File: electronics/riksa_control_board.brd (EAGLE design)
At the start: 69.8 x 70.8 mm, 25 parts

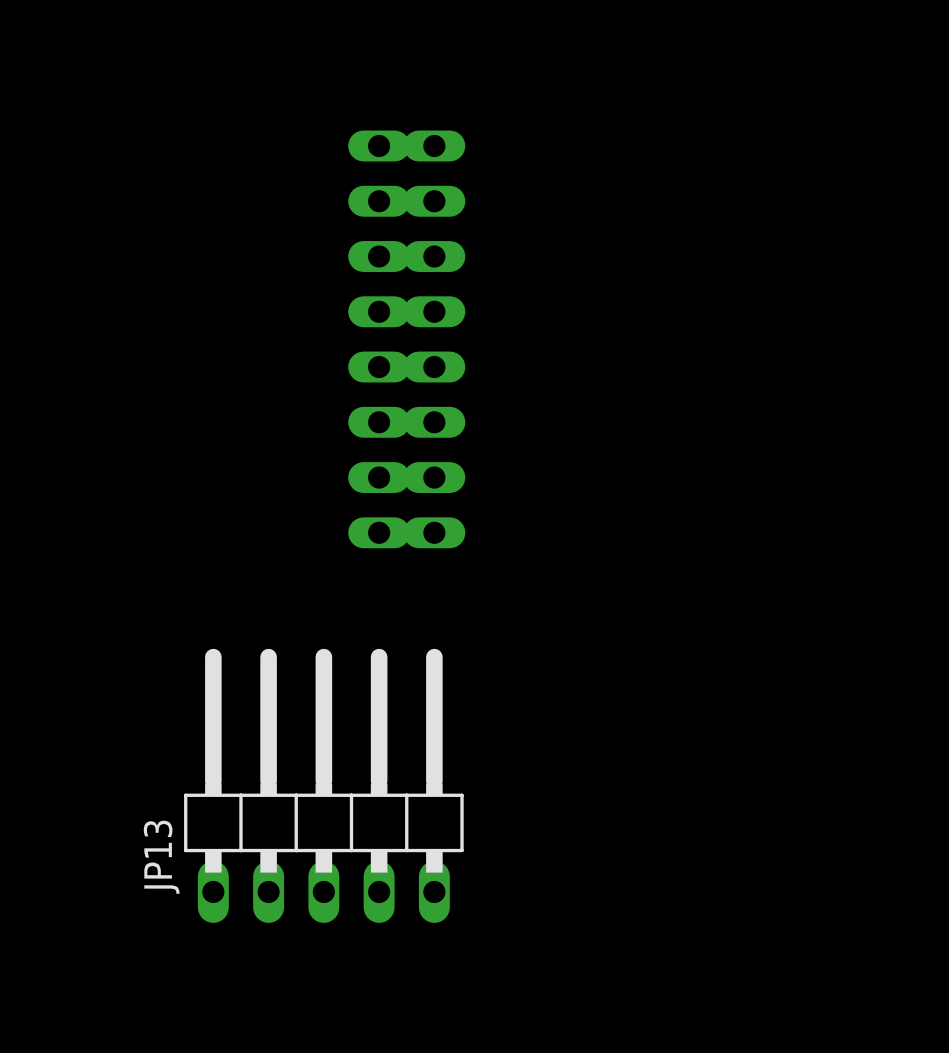
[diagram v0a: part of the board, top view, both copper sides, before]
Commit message: ELE: add rectangle of size the bluetooth module to board
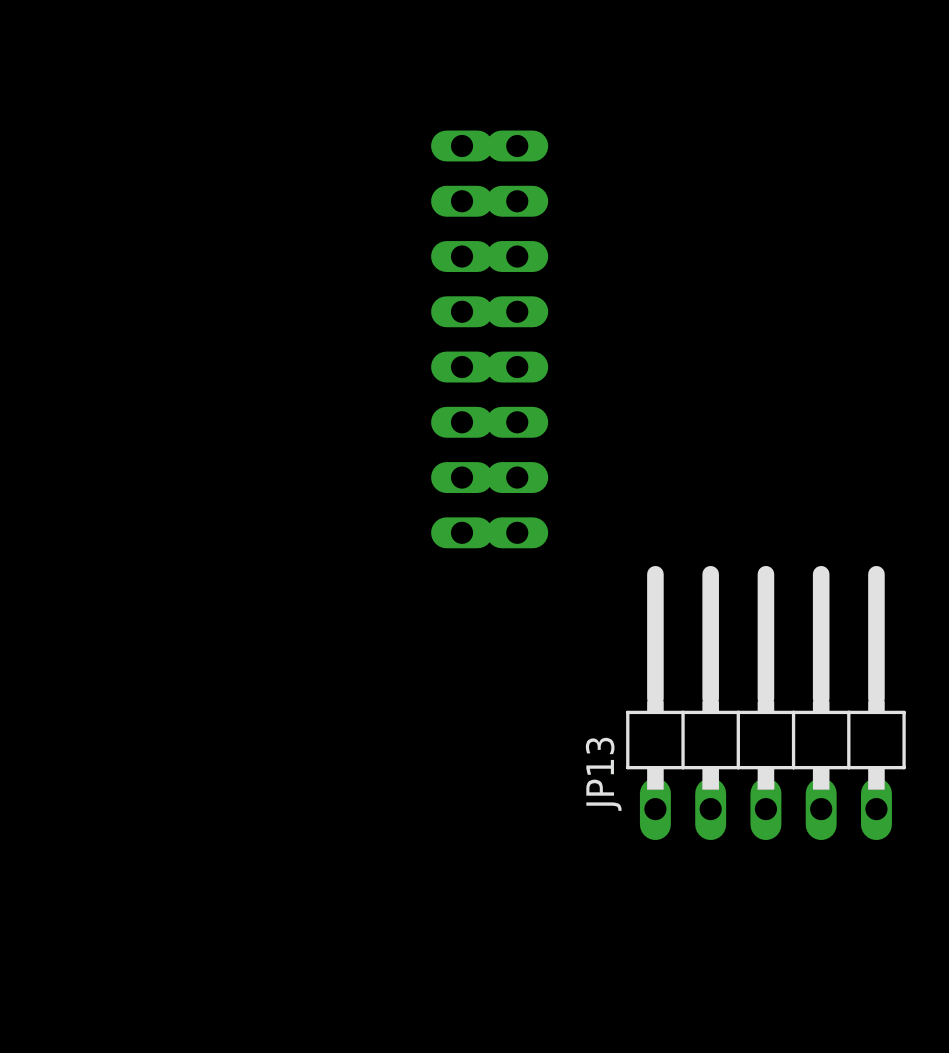
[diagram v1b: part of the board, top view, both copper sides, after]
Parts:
- moved JP13 20.7 mm to (111.8, 11.4)
- moved JP9 6.35 mm to (100.3, 29.2)
- moved JP10 1.27 mm to (97.8, 29.2)
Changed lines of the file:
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@@
 <setting verticaltext="up"/>
 </settings>
-<grid distance="0.05" unitdist="inch" unit="inch" style="lines" multiple="1" display="no" altdistance="0.01" altunitdist="inch" altunit="mm"/>
+<grid distance="0.05" unitdist="inch" unit="mm" style="lines" multiple="1" display="no" altdistance="0.01" altunitdist="inch" altunit="mm"/>
 <layers>
 <layer number="1" name="Top" color="4" fill="1" visible="yes" active="yes"/>
@@
 <hole x="67" y="67" drill="3.2"/>
 <rectangle x1="80.645" y1="21.717" x2="102.235" y2="36.957" layer="52" rot="R270"/>
+<rectangle x1="105.41" y1="10.16" x2="118.11" y2="50.8" layer="48"/>
 </plain>
 <attributes>
@@
 <element name="R4" library="rcl" package="R0805" value="220" x="-50.8" y="109.22"/>
 <element name="R5" library="rcl" package="R0805" value="220" x="-55.88" y="109.22"/>
-<element name="JP9" library="pinhead" library_urn="urn:adsk.eagle:library:325" package="1X08" package3d_urn="urn:adsk.eagle:package:22409/2" value="CON_MPU-6050" x="93.98" y="29.21" rot="MR270"/>
-<element name="JP10" library="pinhead" library_urn="urn:adsk.eagle:library:325" package="1X08" package3d_urn="urn:adsk.eagle:package:22409/2" value="CON_MPU-6050" x="96.52" y="29.21" rot="MR270"/>
+<element name="JP9" library="pinhead" library_urn="urn:adsk.eagle:library:325" package="1X08" package3d_urn="urn:adsk.eagle:package:22409/2" value="CON_MPU-6050" x="100.33" y="29.21" rot="MR270"/>
+<element name="JP10" library="pinhead" library_urn="urn:adsk.eagle:library:325" package="1X08" package3d_urn="urn:adsk.eagle:package:22409/2" value="CON_MPU-6050" x="97.79" y="29.21" rot="MR270"/>
 <element name="R6" library="rcl" package="R0805" value="220" x="13.97" y="34.29" rot="R180"/>
 <element name="JP11" library="pinhead" library_urn="urn:adsk.eagle:library:325" package="2X02" package3d_urn="urn:adsk.eagle:package:22455/2" value="REPRO" x="8.89" y="38.1" rot="R90"/>
 <element name="JP12" library="pinhead" library_urn="urn:adsk.eagle:library:325" package="1X03" package3d_urn="urn:adsk.eagle:package:22458/2" value="VCC_REF_SEL" x="91.44" y="46.99"/>
-<element name="JP13" library="pinhead" library_urn="urn:adsk.eagle:library:325" package="1X05/90" package3d_urn="urn:adsk.eagle:package:22467/2" value="BLUETOOTH" x="91.44" y="7.62"/>
+<element name="JP13" library="pinhead" library_urn="urn:adsk.eagle:library:325" package="1X05/90" package3d_urn="urn:adsk.eagle:package:22467/2" value="BLUETOOTH" x="111.76" y="11.43"/>
 <element name="R7" library="rcl" package="R0805" value="2k2" x="-55.88" y="-38.1"/>
 <element name="R8" library="rcl" package="R0805" value="1k" x="-55.88" y="-44.45"/>
@@
 <contactref element="JP12" pad="2"/>
 <contactref element="JP13" pad="1"/>
-<wire x1="93.98" y1="38.1" x2="96.52" y2="38.1" width="0" layer="19" extent="1-1"/>
-<wire x1="10.16" y1="20.32" x2="93.98" y2="38.1" width="0" layer="19" extent="1-1"/>
+<wire x1="100.33" y1="38.1" x2="97.79" y2="38.1" width="0" layer="19" extent="1-1"/>
+<wire x1="10.16" y1="20.32" x2="100.33" y2="38.1" width="0" layer="19" extent="1-1"/>
 <wire x1="7.62" y1="20.32" x2="10.16" y2="20.32" width="0" layer="19" extent="1-1"/>
 <wire x1="10.16" y1="7.62" x2="10.16" y2="20.32" width="0" layer="19" extent="1-1"/>
 <wire x1="7.62" y1="7.62" x2="10.16" y2="7.62" width="0" layer="19" extent="1-1"/>
 <wire x1="91.44" y1="46.99" x2="7.62" y2="7.62" width="0" layer="19" extent="1-1"/>
-<wire x1="86.36" y1="3.81" x2="91.44" y2="46.99" width="0" layer="19" extent="1-1"/>
+<wire x1="106.68" y1="7.62" x2="91.44" y2="46.99" width="0" layer="19" extent="1-1"/>
 </signal>
 <signal name="GND">
@@
 <contactref element="IM1" pad="14"/>
 <contactref element="R10" pad="2"/>
-<wire x1="93.98" y1="35.56" x2="96.52" y2="35.56" width="0" layer="19" extent="1-1"/>
-<wire x1="45.72" y1="41.91" x2="93.98" y2="35.56" width="0" layer="19" extent="1-1"/>
+<wire x1="100.33" y1="35.56" x2="97.79" y2="35.56" width="0" layer="19" extent="1-1"/>
+<wire x1="45.72" y1="41.91" x2="100.33" y2="35.56" width="0" layer="19" extent="1-1"/>
 <wire x1="40.64" y1="20.32" x2="45.72" y2="41.91" width="0" layer="19" extent="1-1"/>
 <wire x1="25.4" y1="15.24" x2="40.64" y2="20.32" width="0" layer="19" extent="1-1"/>
@@
 <wire x1="10.16" y1="49.53" x2="10.16" y2="25.4" width="0" layer="19" extent="1-1"/>
 <wire x1="7.62" y1="49.53" x2="10.16" y2="49.53" width="0" layer="19" extent="1-1"/>
-<wire x1="88.9" y1="3.81" x2="7.62" y2="12.7" width="0" layer="19" extent="1-1"/>
-<wire x1="-54.93" y1="-38.1" x2="88.9" y2="3.81" width="0" layer="19" extent="1-1"/>
+<wire x1="109.22" y1="7.62" x2="7.62" y2="12.7" width="0" layer="19" extent="1-1"/>
+<wire x1="-54.93" y1="-38.1" x2="109.22" y2="7.62" width="0" layer="19" extent="1-1"/>
 <wire x1="-54.93" y1="-57.15" x2="-54.93" y2="-38.1" width="0" layer="19" extent="1-1"/>
 </signal>
@@
 <contactref element="ARDUINO_NANO1" pad="9"/>
 <contactref element="IM1" pad="36"/>
-<wire x1="93.98" y1="33.02" x2="96.52" y2="33.02" width="0" layer="19" extent="1-1"/>
-<wire x1="25.4" y1="27.94" x2="93.98" y2="33.02" width="0" layer="19" extent="1-1"/>
+<wire x1="100.33" y1="33.02" x2="97.79" y2="33.02" width="0" layer="19" extent="1-1"/>
+<wire x1="25.4" y1="27.94" x2="100.33" y2="33.02" width="0" layer="19" extent="1-1"/>
 <wire x1="20.32" y1="13.97" x2="25.4" y2="27.94" width="0" layer="19" extent="1-1"/>
 </signal>
@@
 <contactref element="ARDUINO_NANO1" pad="8"/>
 <contactref element="IM1" pad="33"/>
-<wire x1="93.98" y1="30.48" x2="96.52" y2="30.48" width="0" layer="19" extent="1-1"/>
-<wire x1="25.4" y1="30.48" x2="93.98" y2="30.48" width="0" layer="19" extent="1-1"/>
+<wire x1="100.33" y1="30.48" x2="97.79" y2="30.48" width="0" layer="19" extent="1-1"/>
+<wire x1="25.4" y1="30.48" x2="100.33" y2="30.48" width="0" layer="19" extent="1-1"/>
 <wire x1="20.32" y1="21.59" x2="25.4" y2="30.48" width="0" layer="19" extent="1-1"/>
 </signal>
@@
 <contactref element="JP9" pad="5"/>
 <contactref element="JP10" pad="5"/>
-<wire x1="93.98" y1="27.94" x2="96.52" y2="27.94" width="0" layer="19" extent="1-1"/>
+<wire x1="100.33" y1="27.94" x2="97.79" y2="27.94" width="0" layer="19" extent="1-1"/>
 </signal>
 <signal name="XCL">
 <contactref element="JP9" pad="6"/>
 <contactref element="JP10" pad="6"/>
-<wire x1="93.98" y1="25.4" x2="96.52" y2="25.4" width="0" layer="19" extent="1-1"/>
+<wire x1="100.33" y1="25.4" x2="97.79" y2="25.4" width="0" layer="19" extent="1-1"/>
 </signal>
 <signal name="AD0">
 <contactref element="JP9" pad="7"/>
 <contactref element="JP10" pad="7"/>
-<wire x1="93.98" y1="22.86" x2="96.52" y2="22.86" width="0" layer="19" extent="1-1"/>
+<wire x1="100.33" y1="22.86" x2="97.79" y2="22.86" width="0" layer="19" extent="1-1"/>
 </signal>
 <signal name="MPU_INT">
@@
 <contactref element="JP9" pad="8"/>
 <contactref element="JP10" pad="8"/>
-<wire x1="93.98" y1="20.32" x2="96.52" y2="20.32" width="0" layer="19" extent="1-1"/>
-<wire x1="40.64" y1="22.86" x2="93.98" y2="20.32" width="0" layer="19" extent="1-1"/>
+<wire x1="100.33" y1="20.32" x2="97.79" y2="20.32" width="0" layer="19" extent="1-1"/>
+<wire x1="40.64" y1="22.86" x2="100.33" y2="20.32" width="0" layer="19" extent="1-1"/>
 </signal>
 <signal name="N$7">
@@
 <contactref element="IM1" pad="34"/>
 <contactref element="ARDUINO_NANO1" pad="17"/>
-<wire x1="20.32" y1="19.05" x2="91.44" y2="3.81" width="0" layer="19" extent="1-1"/>
+<wire x1="20.32" y1="19.05" x2="111.76" y2="7.62" width="0" layer="19" extent="1-1"/>
 <wire x1="40.64" y1="15.24" x2="20.32" y2="19.05" width="0" layer="19" extent="1-1"/>
 </signal>
@@
 <contactref element="JP13" pad="5"/>
 <contactref element="ARDUINO_NANO1" pad="25"/>
-<wire x1="96.52" y1="3.81" x2="40.64" y2="35.56" width="0" layer="19" extent="1-1"/>
+<wire x1="116.84" y1="7.62" x2="40.64" y2="35.56" width="0" layer="19" extent="1-1"/>
 </signal>
 <signal name="TX-&gt;_">
@@
 <contactref element="R7" pad="1"/>
 <wire x1="-56.83" y1="-38.1" x2="-56.83" y2="-44.45" width="0" layer="19" extent="1-1"/>
-<wire x1="93.98" y1="3.81" x2="-56.83" y2="-38.1" width="0" layer="19" extent="1-1"/>
+<wire x1="114.3" y1="7.62" x2="-56.83" y2="-38.1" width="0" layer="19" extent="1-1"/>
 </signal>
 <signal name="VOLTAGE_REF">

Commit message: ELE: final version of control board
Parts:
- added JP14: EMPTY, pinhead:1X02
- moved R8 131.3 mm to (27.3, 57.2), turned to 180 degrees
- moved R7 129.9 mm to (32.4, 57.2)
- moved R10 118.3 mm to (22.9, 31.1), flipped to the bottom, turned to 270 degrees
- moved R4 114.9 mm to (35.6, 33.4), turned to 90 degrees
- moved R9 111.9 mm to (20.3, 31.1), flipped to the bottom, turned to 90 degrees
- moved R3 109.7 mm to (30.5, 30.4), turned to 90 degrees
- moved R5 109.6 mm to (30.5, 41.7), flipped to the bottom, turned to 90 degrees
- moved JP12 90.4 mm to (5.08, 20.3), turned to 90 degrees
- moved JP13 81.5 mm to (41.9, 53.3), flipped to the bottom, turned to 180 degrees
- moved JP9 78.9 mm to (25.4, 4.45), turned to 180 degrees
- moved JP10 77.3 mm to (25.4, 1.99), turned to 180 degrees
- moved JP11 35.4 mm to (43.2, 29.2)
- moved JP2 30.6 mm to (6.35, 53.3), turned to 270 degrees
- moved R6 22.3 mm to (35.6, 28.6), flipped to the bottom, turned to 270 degrees
- moved JP3 20.5 mm to (6.35, 30.5), turned to 270 degrees
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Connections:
- net N$11 renamed D3_BTN_STOP_
- net N$2 renamed D10_REPRO_
- net N$3 renamed D5_LED_FORWADR_
- net N$4 renamed D6_LED_BACKWARD_
- net N$7 renamed D4_BTN_REVERSE_
- net N$8 renamed D9_LED_STOP_
- removed net ROBOCLAW_GND: JP4.3, JP4.4, JP5.3, JP5.4, JP6.3, JP6.4, JP7.3, JP7.4, JP8.3, JP8.4
- removed net ROBOCLAW_GND1: JP11.3, JP11.4
- new net IO18: IM1.30, JP14.2
- new net IO19: IM1.31, JP14.1
- new net N$14: ARDUINO_NANO1.3
- net BT_STATE: now also IM1.3
- net D11_ROBOCLAW_RX: now also IM1.8
- net D12_ROBOCLAW_TX: now also IM1.7
- net D3_BTN_STOP: now also IM1.6
- net D4_BTN_REVERSE: now also IM1.5
- net D5_LED_FORWADR: now also IM1.27
- net D6_LED_BACKWARD: now also IM1.28
- net D9_LED_STOP: now also IM1.26
- net GND: now also JP11.3, JP11.4, JP4.3, JP4.4, JP5.3, JP5.4, JP6.3, JP6.4, JP7.3, JP7.4, JP8.3, JP8.4
- net MPU_INT: now also IM1.4
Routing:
- net VCC: track 0.00 -> 107.2 mm
- net ROBOCLAW_5V: track 0.00 -> 96.4 mm
- net RX<-: track 0.00 -> 86.9 mm, vias 0 -> 2
- net 3V3: track 0.00 -> 82.3 mm
- net D12_ROBOCLAW_TX: track 0.00 -> 82.1 mm
- net D11_ROBOCLAW_RX: track 0.00 -> 81.0 mm
- net TX->: track 0.00 -> 64.4 mm, vias 0 -> 1
- net BT_STATE: track 0.00 -> 64.1 mm, vias 0 -> 2
- net A1_POT_RIGHT: track 0.00 -> 51.5 mm, vias 0 -> 3
- net A0_POT_LEFT: track 0.00 -> 45.1 mm, vias 0 -> 2
- net MPU_SDA: track 0.00 -> 38.9 mm, vias 0 -> 1
- net MPU_SCL: track 0.00 -> 34.5 mm, vias 0 -> 1
- net MPU_INT: track 0.00 -> 31.9 mm
- net VOLTAGE_REF: track 0.00 -> 27.9 mm
- net D5_LED_FORWADR: track 0.00 -> 26.8 mm, vias 0 -> 1
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- added copper zone on layer 1, net GND
- added copper zone on layer 16, net GND
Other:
- board size 69.8 x 70.8 mm -> 50 x 65 mm
- board text added: "+"
- board text added: "-"
- board text added: "18"
- board text added: "3V3"
- board text added: "5V"
- board text added: "B_REV"
- board text added: "B_STOP"
- board text added: "IO:19"
- board text added: "L_B"
- board text added: "L_F"
- board text added: "L_S"
- board text added: "MPU"
- board text added: "P_L"
- board text added: "P_R"
- board text added: "REP"
- board text added: "ROBOCLAW"
- board text added: "RX"
- board text added: "Riksa Control Board v1.0 J.Paral, P.Bobcik"
- board text added: "Robotarna RobotikaBrno"
- board text added: "S"
- board text added: "ST"
- board text added: "TX"
- board text added: "VCC"
- board text added: "VCC_REF"

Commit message: ELE: fix Kubas comments
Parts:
- added C1: 470u/10V, rcl:TT5D6
- added C2: 4u7/10V, rcl:C0805
- added C3, C4: 100n/10V, rcl:C0603
- added D1, D2, D3, D5, D6: Schottky, diode:D0603
- added JP15: LEDS, pinhead:1X02
- added LED1: green, led:CHIPLED_0603
- added LED2: red, led:CHIPLED_0603
- added LED3: yellow, led:CHIPLED_0603
- added R11, R14, R17, R20, R21: 1k, rcl:R0805
- added R12, R13: 220, rcl:R0805
- added R15, R16, R18, R19: 4k7, rcl:R0805
- R8: value 1k -> 220
- moved R8 48.4 mm to (-19.1, 71.1), turned to 0 degrees
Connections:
- removed net 3V3: ARDUINO_NANO1.2, IM1.1, JP12.1
- removed net N$14: ARDUINO_NANO1.3
- removed net ROBOCLAW_5V: ARDUINO_NANO1.12, IM1.19, JP1.1, JP1.2, JP12.3, R9.1
- new net +3V3: ARDUINO_NANO1.2, IM1.1, JP12.1, R7.2
- new net +5V: ARDUINO_NANO1.12, C1.+, C2.1, C3.1, IM1.19, JP1.1, JP1.2, JP12.3, R17.2, R9.1
- new net A0_POT_LEFT_: JP3.3, JP3.4, R8.1
- new net A1_POT_RIGHT_: JP2.3, JP2.4, R12.1
- new net D11_ROBOCLAW_RX_: JP1.7, JP1.8, R11.2
- new net D12_ROBOCLAW_TX_: JP1.5, JP1.6, R14.2
- new net LED_GREEN_: LED1.C, R17.1
- new net LED_RED: JP15.1, R20.1
- new net LED_RED_: LED2.C, R20.2
- new net LED_YELLOW: JP15.2, R21.1
- new net LED_YELLOW_: LED3.C, R21.2
- new net N$3: IM1.37
- new net N$4: IM1.15
- new net N$7: ARDUINO_NANO1.3, C4.2
- new net RX<-_: JP13.3, R13.2
- net A0_POT_LEFT: now also R8.2; no longer JP3.3, JP3.4
- net A1_POT_RIGHT: now also R12.2; no longer JP2.3, JP2.4
- net D11_ROBOCLAW_RX: now also D2.A, D3.A, R11.1; no longer JP1.7, JP1.8
- net D12_ROBOCLAW_TX: now also D5.A, D6.A, R14.1; no longer JP1.5, JP1.6
- net D3_BTN_STOP: now also R19.2
- net D4_BTN_REVERSE: now also R18.2
- net GND: now also C1.-, C2.2, C3.2, C4.1, D3.C, D6.C, LED1.A, LED2.A, LED3.A; no longer R7.2
- net MPU_SCL: now also R16.2
- net MPU_SDA: now also R15.2
- net RX<-: now also R13.1; no longer JP13.3
- net TX->: now also D1.C; no longer R8.2
- net TX->_: now also D1.A; no longer R8.1
- net VCC: now also D2.C, D5.C, R15.1, R16.1, R18.1, R19.1
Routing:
- net ROBOCLAW_5V: track 96.4 -> 0.00 mm
- net +5V: track 0.00 -> 87.7 mm
- net 3V3: track 82.3 -> 0.00 mm
- net +3V3: track 0.00 -> 77.6 mm
- net D11_ROBOCLAW_RX: track 81.0 -> 53.8 mm
- net D12_ROBOCLAW_TX: track 82.1 -> 71.1 mm
- net A0_POT_LEFT: track 45.1 -> 36.8 mm
- net A1_POT_RIGHT: track 51.5 -> 47.1 mm
- net TX->_: track 18.2 -> 15.0 mm
- net D12_ROBOCLAW_TX_: track 0.00 -> 2.54 mm
- net D11_ROBOCLAW_RX_: track 0.00 -> 2.54 mm
- net A1_POT_RIGHT_: track 0.00 -> 2.54 mm
- net A0_POT_LEFT_: track 0.00 -> 2.54 mm
- net GND: track 14.7 -> 12.9 mm
- net TX->: track 64.4 -> 63.1 mm
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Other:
- outline, holes or cut-outs redrawn
